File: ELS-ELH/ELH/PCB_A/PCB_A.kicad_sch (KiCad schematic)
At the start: 44 parts, among them J1 Conn_01x08_Pin, J3 Conn_01x20_Pin, J4 Conn_01x20_Pin, Q1 IRLZ44N, Q2 IRLZ44N, Q4 IRLZ44N, Q6 IRLZ44N

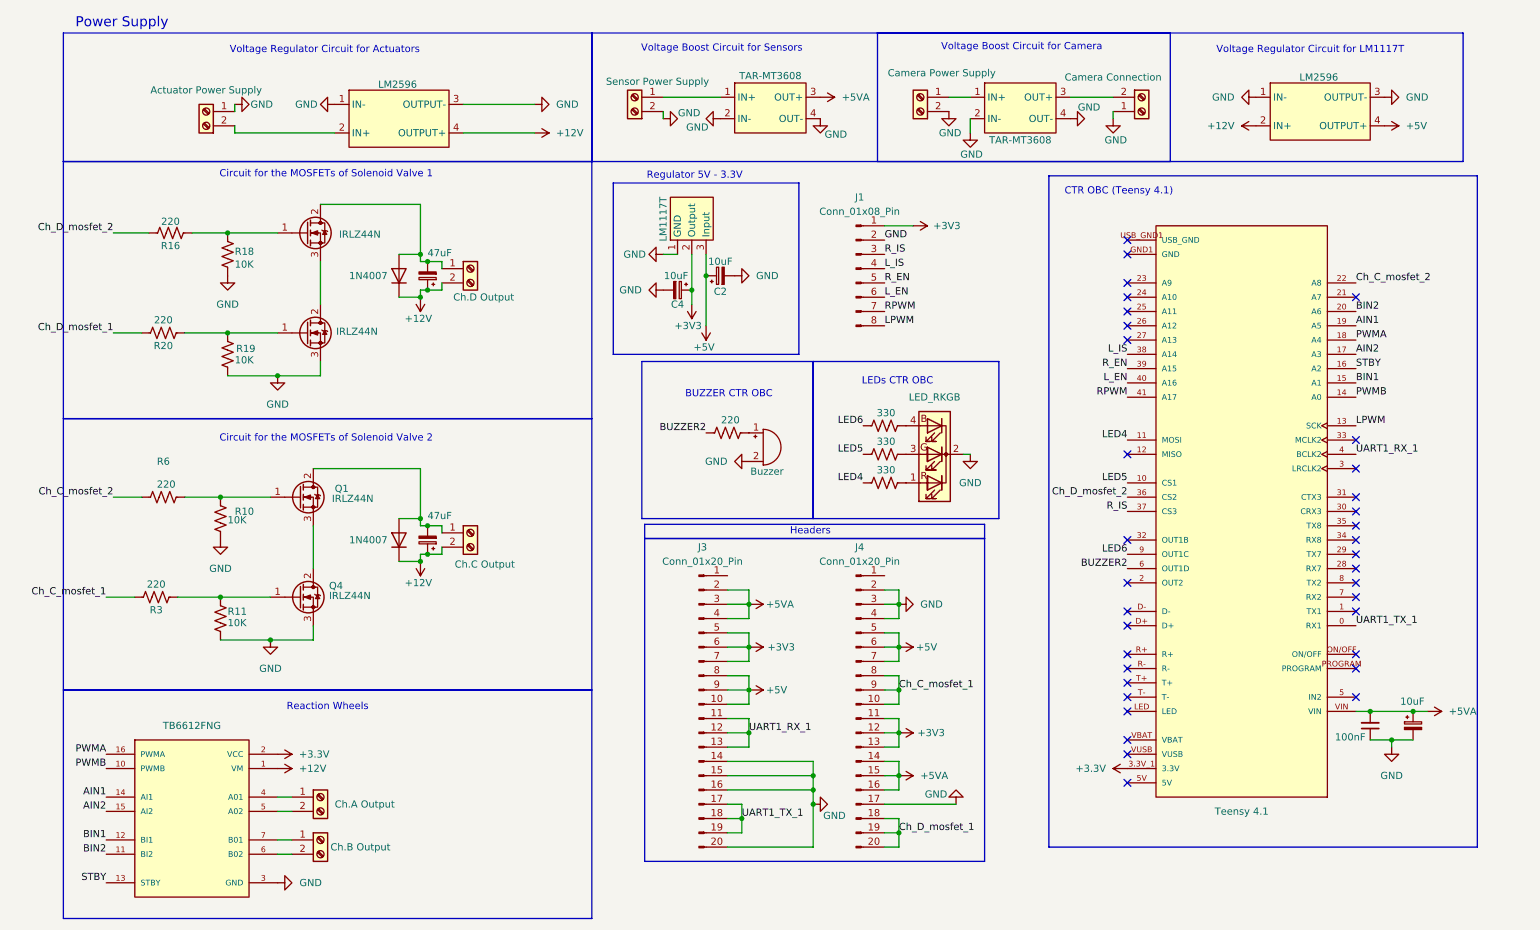
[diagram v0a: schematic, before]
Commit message: General Update
Final version & manufacture files of both PCBs + codes of unit testing on modules and functionalities

* Update on net labels of both PCBs

* Update in symbols and footprints

* Unitary Tests Codes

* Update on schematics B

* Update in PCB B - new layout

* Update in schematic A

* PCB B Almost finishhed

* PCB B ready, PCB A layout ready

* Finish PCB B

* Solve DRC problems with B

* PCB A routed

* reorganized resistances

* regulator's names changed

* Update almost finished

* Finished the manufacture

---------

Co-authored-by: sofiamelo02 <sofia.melo@udea.edu.co>
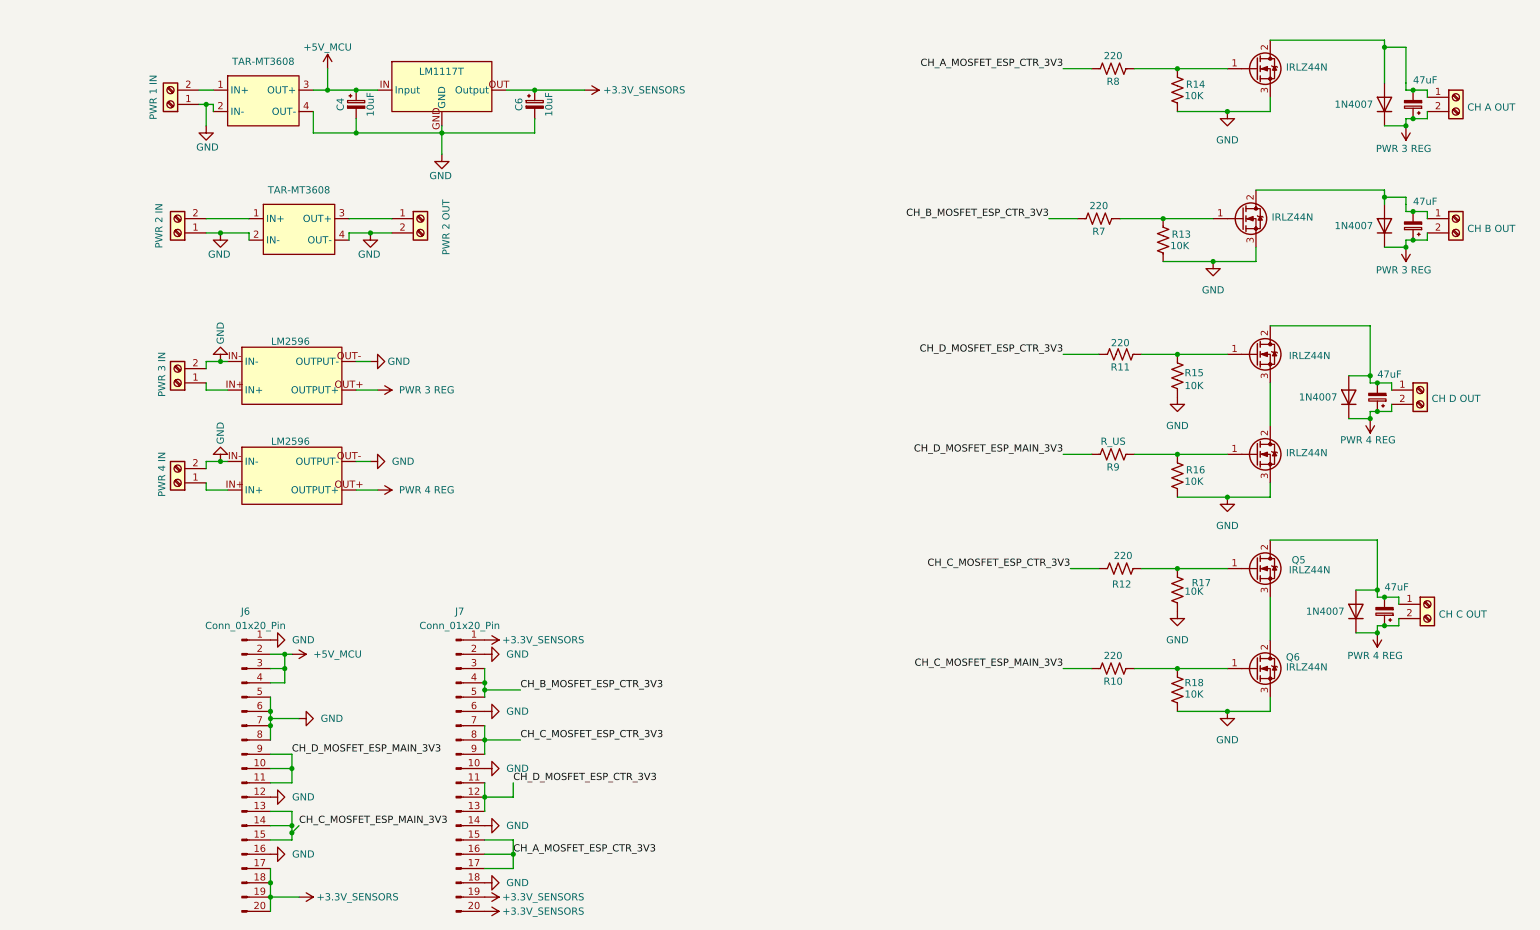
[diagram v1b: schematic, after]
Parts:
- removed BOOST1, BOOST2: TAR-MT3608, ELH_Library:TAR-MT3608, symbol ELH_Library:XL6009_Boost
- removed BZ2: Buzzer, Buzzer_Beeper:Buzzer_12x9.5RM7.6, symbol Device:Buzzer
- removed Bornera1: Camera Connection, ELH_Library:Bornera 2P, symbol Connector:Screw_Terminal_01x02
- removed Bornera2: Ch.A Output, ELH_Library:Bornera 2P, symbol Connector:Screw_Terminal_01x02
- removed Bornera6: Sensor Power Supply, ELH_Library:Bornera 2P, symbol Connector:Screw_Terminal_01x02
- removed Bornera7: Ch.B Output, ELH_Library:Bornera 2P, symbol Connector:Screw_Terminal_01x02
- removed Bornera8: Camera Power Supply, ELH_Library:Bornera 2P, symbol Connector:Screw_Terminal_01x02
- removed C1: 100nF, Capacitor_THT:C_Disc_D5.0mm_W2.5mm_P5.00mm, symbol Device:C_Small
- removed C2: 10uF, Capacitor_THT:CP_Radial_D5.0mm_P2.00mm, symbol Device:C_Polarized_Small
- removed C3: 10uF, Capacitor_THT:CP_Radial_D5.0mm_P2.50mm, symbol Device:C_Polarized_Small
- removed D3: LED_RKGB, LED_THT:LED_D5.0mm-4_RGB_Staggered_Pins, symbol Device:LED_RKGB
- removed Driver_DC2: TB6612FNG, ELH_Library:TB6612FNG, symbol ELH_Library:TB6612FNG
- removed J1: Conn_01x08_Pin, Connector_PinSocket_2.54mm:PinSocket_1x08_P2.54mm_Vertical, symbol Connector:Conn_01x08_Pin
- removed J3, J4: Conn_01x20_Pin, Connector_PinSocket_2.54mm:PinSocket_1x20_P2.54mm_Vertical, symbol Connector:Conn_01x20_Pin
- removed R1, R2: 330, Resistor_THT:R_Axial_DIN0207_L6.3mm_D2.5mm_P7.62mm_Horizontal, symbol Device:R_US
- removed R9: 220, Resistor_THT:R_Axial_DIN0207_L6.3mm_D2.5mm_P7.62mm_Horizontal, symbol Device:R_US
- removed Regulator1: LM1117T, ELH_Library:LM1117T, symbol ELH_Library:LM1117T
- removed Regulator3: LM2596, ELH_Library:LM2596, symbol ELH_Library:MP1584
- removed Teensy3: Teensy 4.1, ELH_Library:Teensy 4.1, symbol ELH_Library:Teensy 4.1
- added BOOST1, BOOST2: TAR-MT3608, ELH_Library:TAR-MT3608, symbol ELH_Library:TAR-MT3608
- added C10, C9: 47uF, Capacitor_THT:CP_Radial_D6.3mm_P2.50mm, symbol Device:C_Polarized_Small
- added C6: 10uF, Capacitor_THT:CP_Radial_D5.0mm_P2.00mm, symbol Device:C_Polarized_Small
- added D4, D5: 1N4007, Diode_THT:D_DO-41_SOD81_P10.16mm_Horizontal, symbol Diode:1N4007
- added J1: PWR 1 IN, ELH_Library:Bornera 2P, symbol Connector:Screw_Terminal_01x02
- added J11: CH A OUT, ELH_Library:Bornera 2P, symbol Connector:Screw_Terminal_01x02
- added J12: CH B OUT, ELH_Library:Bornera 2P, symbol Connector:Screw_Terminal_01x02
- added J2: PWR 2 IN, ELH_Library:Bornera 2P, symbol Connector:Screw_Terminal_01x02
- added J4: PWR 4 IN, ELH_Library:Bornera 2P, symbol Connector:Screw_Terminal_01x02
- added J5: PWR 2 OUT, ELH_Library:Bornera 2P, symbol Connector:Screw_Terminal_01x02
- added J6, J7: Conn_01x20_Pin, Connector_PinHeader_2.54mm:PinHeader_1x20_P2.54mm_Vertical, symbol Connector:Conn_01x20_Pin
- added Q1, Q2: IRLZ44N, Package_TO_SOT_THT:TO-220-3_Vertical, symbol Transistor_FET:IRLZ44N
- added R13, R14: 10K, Resistor_THT:R_Axial_DIN0207_L6.3mm_D2.5mm_P7.62mm_Horizontal, symbol Device:R_US
- added R7: 220, Resistor_THT:R_Axial_DIN0207_L6.3mm_D2.5mm_P7.62mm_Horizontal, symbol Device:R_US
- added Regulator2: LM2596, ELH_Library:LM2596, symbol ELH_Library:MP1584
- added Regulator3: LM1117T, ELH_Library:LM1117T, symbol ELH_Library:LM1117T
- J10: renamed from Bornera4; value Ch.C Output -> CH C OUT
- J3: renamed from Bornera3; value Actuator Power Supply -> PWR 3 IN
- J9: renamed from Bornera5; value Ch.D Output -> CH D OUT
- R8: value 330 -> 220
- R9: renamed from R20; value 220 -> R_US
- renumbered C9 to C7, C10 to C8, D9 to D2, D1 to D3, Q6 to Q3, Q2 to Q4, Q1 to Q5, Q4 to Q6, R3 to R10, R16 to R11, R6 to R12, R18 to R15, R19 to R16, R10 to R17, R11 to R18, Regulator4 to Regulator1
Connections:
- net GND: now also J3.2 (Pin_2), Regulator1.IN-, Regulator1.OUT- (OUTPUT-), BOOST1.2 (IN-), BOOST1.4 (OUT-), BOOST2.2 (IN-), BOOST2.4 (OUT-), C6.2, J1.1 (Pin_1), J2.1 (Pin_1), J4.2 (Pin_2), J5.2 (Pin_2), J6.1 (Pin_1), J6.12 (Pin_12), J6.16 (Pin_16), J6.5 (Pin_5), J6.6 (Pin_6), J6.7 (Pin_7), J6.8 (Pin_8), J7.10 (Pin_10), J7.14 (Pin_14), J7.18 (Pin_18), J7.2 (Pin_2), J7.6 (Pin_6), Q1.3 (S), Q2.3 (S), R13.2, R14.2, Regulator2.IN-, Regulator2.OUT- (OUTPUT-), Regulator3.GND; no longer J3.1 (Pin_2), Regulator1.1 (IN-), Regulator1.3 (OUTPUT-)
- net CH_A_MOSFET_ESP_CTR_3V3: now reaches R8.1
- net CH_A_MOSFET_ESP_CTR_3V3: now also J7.15 (Pin_15), J7.16 (Pin_16), J7.17 (Pin_17)
- net +12V renamed PWR 4 REG
- net PWR 4 REG: now also Regulator2.OUT+ (OUTPUT+); no longer Regulator1.4 (OUTPUT+)
- net +3V3 renamed +5V_MCU
- net +5V_MCU: now also BOOST1.3 (OUT+), J6.2 (Pin_2), J6.3 (Pin_3), J6.4 (Pin_4), Regulator3.IN (Input)
- net Ch_C_mosfet_1 renamed CH_C_MOSFET_ESP_MAIN_3V3
- net CH_C_MOSFET_ESP_MAIN_3V3: now also J6.13 (Pin_13), J6.14 (Pin_14), J6.15 (Pin_15)
- net Ch_C_mosfet_2 renamed CH_C_MOSFET_ESP_CTR_3V3
- net CH_C_MOSFET_ESP_CTR_3V3: now also J7.7 (Pin_7), J7.8 (Pin_8), J7.9 (Pin_9)
- net Ch_D_mosfet_1 renamed CH_D_MOSFET_ESP_MAIN_3V3
- net CH_D_MOSFET_ESP_MAIN_3V3: now also J6.10 (Pin_10), J6.11 (Pin_11), J6.9 (Pin_9)
- net Ch_D_mosfet_2 renamed CH_D_MOSFET_ESP_CTR_3V3
- net CH_D_MOSFET_ESP_CTR_3V3: now also J7.11 (Pin_11), J7.12 (Pin_12), J7.13 (Pin_13)
- net LED4: no longer names the net of R8.2
- net LED4: now also Q2.1 (G), R14.1
- new net: BOOST1.1 (IN+), J1.2 (Pin_2)
- new net: J3.1 (Pin_1), Regulator1.IN+
- new net: BOOST2.1 (IN+), J2.2 (Pin_2)
- new net: BOOST2.3 (OUT+), J5.1 (Pin_1)
- new net: C9.2, D4.2 (A), J11.1 (Pin_1), Q2.2 (D)
- new net: J4.1 (Pin_1), Regulator2.IN+
- new net: Q1.1 (G), R13.1, R7.2
- new net: C10.2, D5.2 (A), J12.1 (Pin_1), Q1.2 (D)
- new net +3.3V_SENSORS: C6.1, J6.17 (Pin_17), J6.18 (Pin_18), J6.19 (Pin_19), J6.20 (Pin_20), J7.1 (Pin_1), J7.19 (Pin_19), J7.20 (Pin_20), Regulator3.OUT (Output)
- new net CH_B_MOSFET_ESP_CTR_3V3: J7.3 (Pin_3), J7.4 (Pin_4), J7.5 (Pin_5), R7.1
- new net PWR 3 REG: C10.1, C9.1, D4.1 (K), D5.1 (K), J11.2 (Pin_2), J12.2 (Pin_2), Regulator1.OUT+ (OUTPUT+)
- no-connect marks 35 -> 0
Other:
- note removed: "BUZZER CTR OBC"
- note removed: "CTR OBC (Teensy 4.1)"
- note removed: "Circuit for the MOSFETs of Solenoid Valve 1"
- note removed: "Circuit for the MOSFETs of Solenoid Valve 2"
- note removed: "Headers"
- note removed: "LEDs CTR OBC"
- note removed: "Power Supply"
- note removed: "Reaction Wheels"
- note removed: "Regulator 5V - 3.3V"
- note removed: "Voltage Boost Circuit for Camera"
- note removed: "Voltage Boost Circuit for Sensors"
- note removed: "Voltage Regulator Circuit for Actuators"
- note removed: "Voltage Regulator Circuit for LM1117T"
- moved on the sheet: Q5, Q6, R10, R11, R12, R15, R16, R17, R18, R9
